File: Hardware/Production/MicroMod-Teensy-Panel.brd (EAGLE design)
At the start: 199.6 x 83.1 mm, 1190 parts, among them J1 MICROMOD-2222, J10 MICROMOD-2222, J11 MICROMOD-2222, J12 MICROMOD-2222, J13 MICROMOD-2222, J14 MICROMOD-2222, J15 MICROMOD-2222, J16 MICROMOD-2222, J2 MICROMOD-2222, J3 MICROMOD-2222, J4 MICROMOD-2222, J5 MICROMOD-2222, J6 MICROMOD-2222, J7 MICROMOD-2222, J8 MICROMOD-2222, J9 MICROMOD-2222, Q1 20V/4.2A/52mΩ/1.4W, Q10 20V/0.2A/8MHz/1.2Ω/1Vth, Q11 20V/4.2A/52mΩ/1.4W, Q12 20V/0.2A/8MHz/1.2Ω/1Vth, Q13 20V/4.2A/52mΩ/1.4W, Q14 20V/0.2A/8MHz/1.2Ω/1Vth, Q15 20V/4.2A/52mΩ/1.4W, Q16 20V/0.2A/8MHz/1.2Ω/1Vth, Q17 20V/4.2A/52mΩ/1.4W, Q18 20V/0.2A/8MHz/1.2Ω/1Vth, Q19 20V/4.2A/52mΩ/1.4W, Q2 20V/0.2A/8MHz/1.2Ω/1Vth, Q20 20V/0.2A/8MHz/1.2Ω/1Vth, Q21 20V/4.2A/52mΩ/1.4W, Q22 20V/0.2A/8MHz/1.2Ω/1Vth, Q23 20V/4.2A/52mΩ/1.4W, Q24 20V/0.2A/8MHz/1.2Ω/1Vth, Q25 20V/4.2A/52mΩ/1.4W, Q26 20V/0.2A/8MHz/1.2Ω/1Vth, Q27 20V/4.2A/52mΩ/1.4W, Q28 20V/0.2A/8MHz/1.2Ω/1Vth, Q29 20V/4.2A/52mΩ/1.4W, Q3 20V/4.2A/52mΩ/1.4W, Q30 20V/0.2A/8MHz/1.2Ω/1Vth, Q31 20V/4.2A/52mΩ/1.4W, Q32 20V/0.2A/8MHz/1.2Ω/1Vth, Q4 20V/0.2A/8MHz/1.2Ω/1Vth, Q5 20V/4.2A/52mΩ/1.4W, Q6 20V/0.2A/8MHz/1.2Ω/1Vth, Q7 20V/4.2A/52mΩ/1.4W, Q8 20V/0.2A/8MHz/1.2Ω/1Vth, Q9 20V/4.2A/52mΩ/1.4W, U1 IMXRT1062DV10X10, U10 IMXRT1062DV10X10, U11 W25QXX3X2, U12 MKL02Z32VFG4, U13 IMXRT1062DV10X10, U14 W25QXX3X2, U15 MKL02Z32VFG4, U16 IMXRT1062DV10X10, U17 W25QXX3X2, U18 MKL02Z32VFG4, U19 IMXRT1062DV10X10, U2 W25QXX3X2, U20 W25QXX3X2, U21 MKL02Z32VFG4, U22 IMXRT1062DV10X10, U23 W25QXX3X2, U24 MKL02Z32VFG4, U25 IMXRT1062DV10X10, U26 W25QXX3X2, U27 MKL02Z32VFG4, U28 IMXRT1062DV10X10, U29 W25QXX3X2, U3 MKL02Z32VFG4, U30 MKL02Z32VFG4, U31 IMXRT1062DV10X10, U32 W25QXX3X2, U33 MKL02Z32VFG4, U34 IMXRT1062DV10X10, U35 W25QXX3X2, U36 MKL02Z32VFG4, U37 IMXRT1062DV10X10, U38 W25QXX3X2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

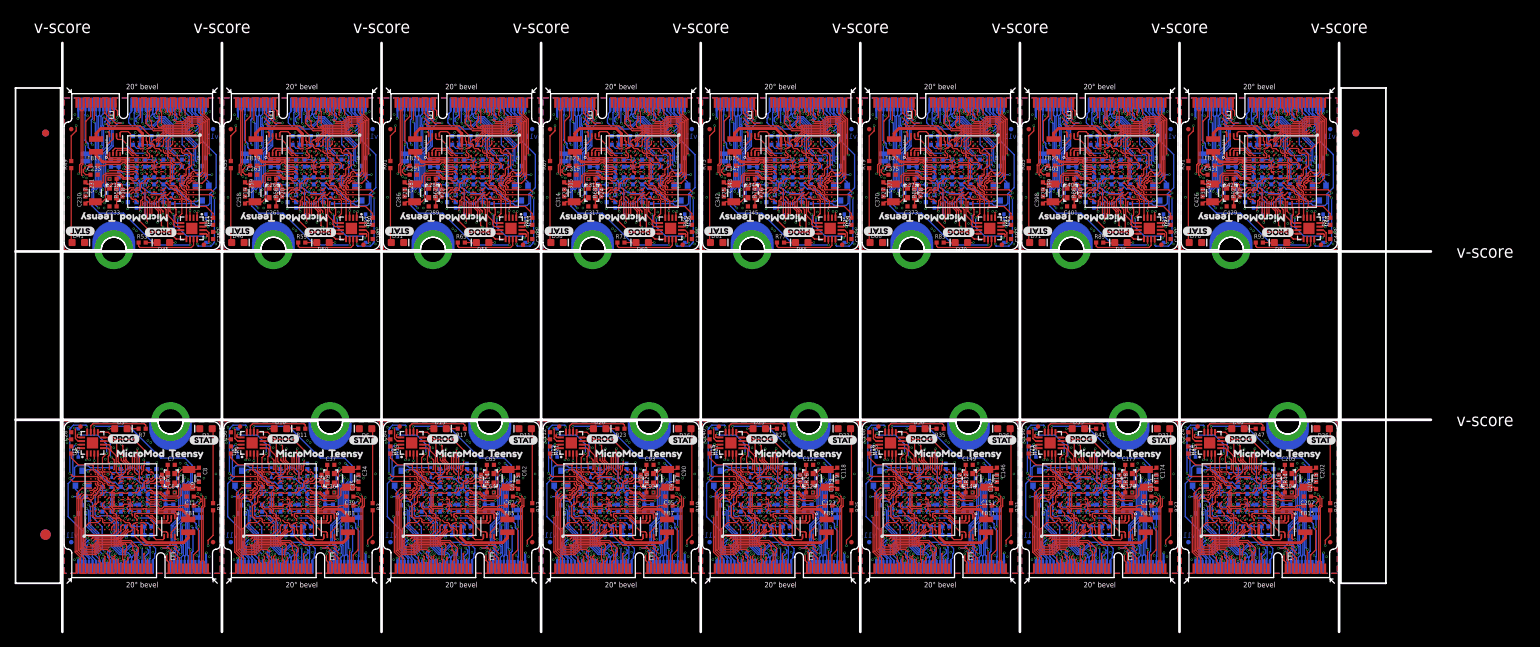
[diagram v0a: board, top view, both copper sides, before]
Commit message: Matches trace lenths to flash. New panel.
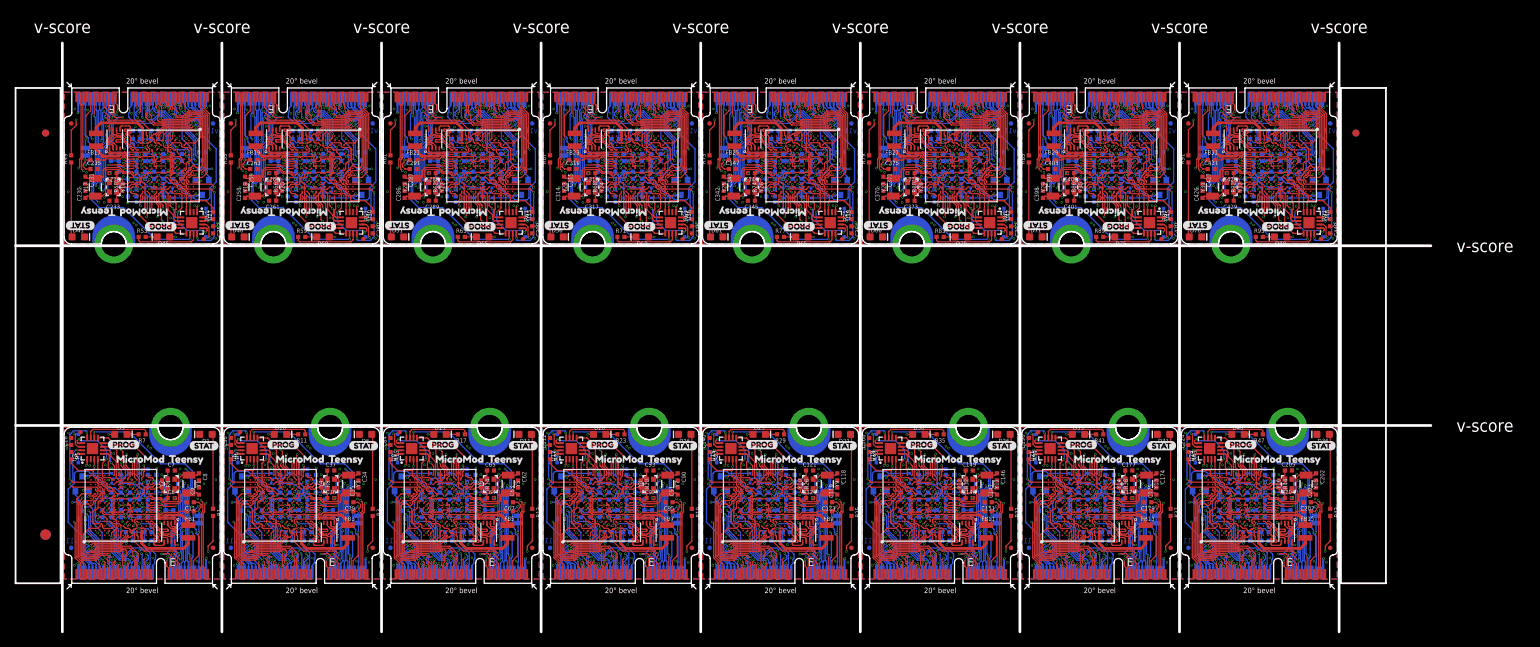
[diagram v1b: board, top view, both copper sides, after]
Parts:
- TP1, TP100, TP111, TP12, TP122, TP133, TP144, TP155, TP166, TP23, TP34, TP45, TP56, TP67, TP78, TP89: value 32kHz Test -> (none)
- TP10, TP101, TP102, TP103, TP104, TP105, TP106, TP107, TP108, TP109, TP11, TP110, TP112, TP113, TP114, TP115, TP116, TP117, TP118, TP119, TP120, TP121, TP123, TP124, TP125, TP126, TP127, TP128, TP129, TP13, TP130, TP131, TP132, TP134, TP135, TP136, TP137, TP138, TP139, TP14, TP140, TP141, TP142, TP143, TP145, TP146, TP147, TP148, TP149, TP15, TP150, TP151, TP152, TP153, TP154, TP156, TP157, TP158, TP159, TP16, TP160, TP161, TP162, TP163, TP164, TP165, TP167, TP168, TP169, TP17, TP170, TP171, TP172, TP173, TP174, TP175, TP176, TP18, TP19, TP2, TP20, TP21, TP22, TP24, TP25, TP26, TP27, TP28, TP29, TP3, TP30, TP31, TP32, TP33, TP35, TP36, TP37, TP38, TP39, TP4, TP40, TP41, TP42, TP43, TP44, TP46, TP47, TP48, TP49, TP5, TP50, TP51, TP52, TP53, TP54, TP55, TP57, TP58, TP59, TP6, TP60, TP61, TP62, TP63, TP64, TP65, TP66, TP68, TP69, TP7, TP70, TP71, TP72, TP73, TP74, TP75, TP76, TP77, TP79, TP8, TP80, TP81, TP82, TP83, TP84, TP85, TP86, TP87, TP88, TP9, TP90, TP91, TP92, TP93, TP94, TP95, TP96, TP97, TP98, TP99: value TEST-POINT2 -> (none)
- moved C11 0.80 mm to (17.8, 11.4)
- moved C112 0.80 mm to (68.5, 20.0)
- moved C118 0.80 mm to (109.0, 15.0)
- moved C119 0.80 mm to (109.0, 13.0)
- moved C120 0.80 mm to (105.1, 12.0)
- moved C123 0.80 mm to (107.8, 11.4)
- moved C140 0.80 mm to (91.0, 20.0)
- moved C146 0.80 mm to (131.5, 15.0)
- moved C147 0.80 mm to (131.5, 13.0)
- moved C148 0.80 mm to (127.6, 12.0)
- moved C151 0.80 mm to (130.3, 11.4)
- moved C168 0.80 mm to (113.5, 20.0)
- moved C174 0.80 mm to (154.1, 15.0)
- moved C175 0.80 mm to (154.1, 13.0)
- moved C176 0.80 mm to (150.2, 12.0)
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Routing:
- net QSPI6: track 3.16 -> 7.39 mm
- net QSPI42: track 3.16 -> 7.39 mm
- net QSPI62: track 3.16 -> 7.39 mm
- net QSPI58: track 3.16 -> 7.39 mm
- net QSPI34: track 3.16 -> 7.39 mm
- net QSPI30: track 3.16 -> 7.39 mm
- net QSPI26: track 3.16 -> 7.39 mm
- net QSPI2: track 3.16 -> 7.39 mm
- net QSPI38: track 3.16 -> 7.39 mm
- net QSPI10: track 3.16 -> 7.39 mm
- net QSPI50: track 3.16 -> 7.39 mm
- net QSPI18: track 3.16 -> 7.39 mm
- net QSPI54: track 3.16 -> 7.39 mm
- net QSPI46: track 3.16 -> 7.39 mm
- net QSPI22: track 3.16 -> 7.39 mm
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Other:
- outline, holes or cut-outs redrawn

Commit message: Route bus pins to v11.
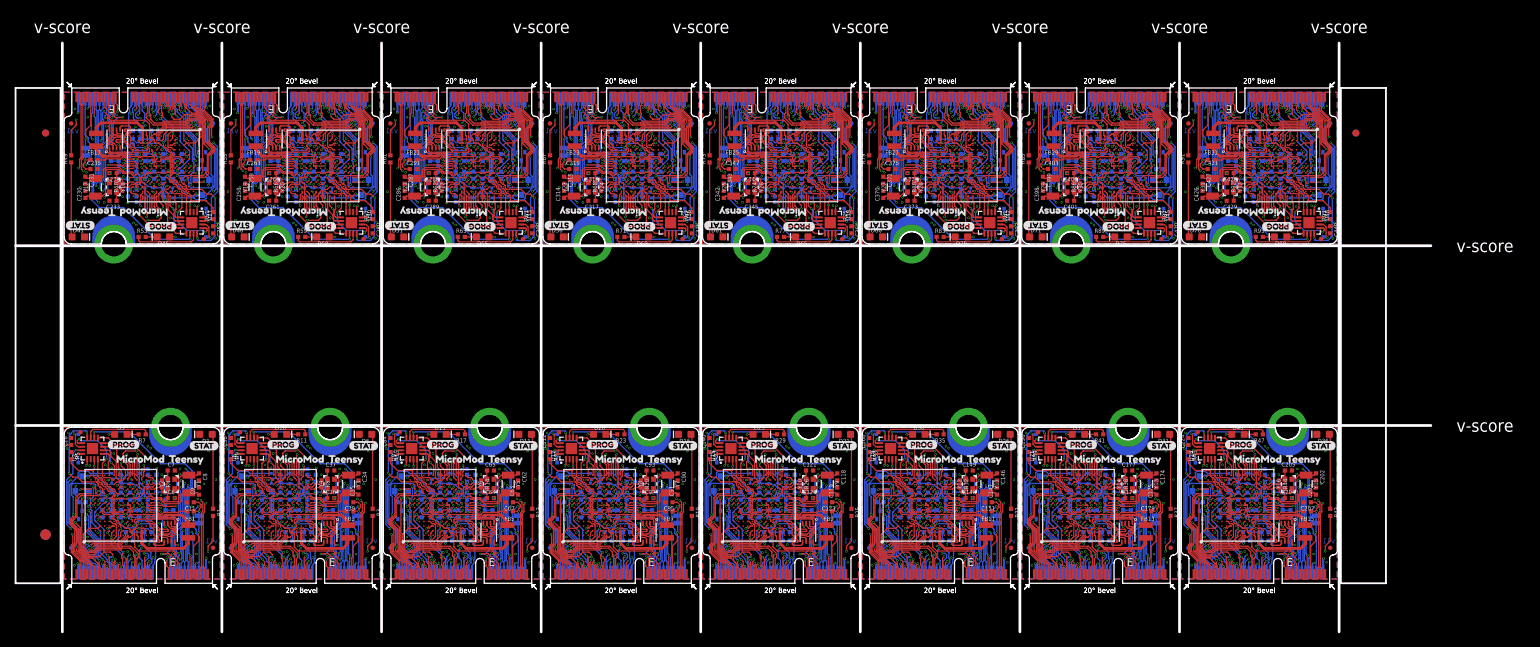
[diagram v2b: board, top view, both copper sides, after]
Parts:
- added FRAME1, FRAME10, FRAME11, FRAME12, FRAME13, FRAME14, FRAME15, FRAME16, FRAME2, FRAME3, FRAME4, FRAME5, FRAME6, FRAME7, FRAME8, FRAME9: FRAME-LEDGER, SparkFun-Aesthetics:CREATIVE_COMMONS
- added LOGO17, LOGO19, LOGO21, LOGO23, LOGO25, LOGO27, LOGO29, LOGO31: SFE_LOGO_NAME_FLAME.1_INCH, SparkFun-Aesthetics:SFE_LOGO_NAME_FLAME_.1
- added LOGO18, LOGO20, LOGO22, LOGO24, LOGO26, LOGO28, LOGO30, LOGO32: OSHW-LOGONO_SILK, SparkFun-Aesthetics:DUMMY
- LOGO10, LOGO12, LOGO14, LOGO16, LOGO2, LOGO4, LOGO6, LOGO8: value SFE_LOGO_NAME_FLAME.1_INCH -> OSHW-LOGONO_SILK; device SparkFun-Aesthetics:SFE_LOGO_NAME_FLAME_.1 -> SparkFun-Aesthetics:DUMMY
- moved LOGO8 116.0 mm to (55.7, -22.9), flipped to the top
- moved LOGO6 95.3 mm to (33.2, -22.9), flipped to the top
- moved LOGO9 88.1 mm to (96.7, 18.1), turned to 0 degrees
- moved LOGO10 84.8 mm to (78.2, -22.9), flipped to the top, turned to 0 degrees
- moved LOGO16 79.4 mm to (145.7, -22.9), flipped to the top, turned to 0 degrees
- moved LOGO12 76.7 mm to (100.7, -22.9), flipped to the top, turned to 0 degrees
- moved LOGO4 75.6 mm to (10.7, -22.9), flipped to the top
- moved LOGO14 74.8 mm to (123.2, -22.9), flipped to the top, turned to 0 degrees
- moved LOGO11 67.9 mm to (119.2, 18.1), turned to 0 degrees
- moved LOGO7 67.5 mm to (74.2, 18.1)
- moved LOGO2 58.0 mm to (-11.8, -22.9), flipped to the top
- moved LOGO13 49.6 mm to (141.8, 18.1), turned to 0 degrees
- moved LOGO5 45.0 mm to (51.7, 18.1)
- moved LOGO15 36.4 mm to (164.3, 18.1), turned to 0 degrees
- moved LOGO3 22.5 mm to (29.2, 18.1)
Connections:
- new net GPIO/100: J10.69, U28.A10
- new net GPIO/101: J10.71, U28.D9
- new net GPIO/102: U28.D5
- new net GPIO/103: J10.65, U28.C10
- new net GPIO/104: J10.63, U28.H4
- new net GPIO/105: J10.40, U28.C8
- new net GPIO/106: J10.42, U28.B8
- new net GPIO/107: J10.44, U28.A8
- new net GPIO/108: J10.46, U28.A9
- new net GPIO/109: J10.48, U28.B9
- new net GPIO/110: J10.73, U28.C9
- new net GPIO/111: J11.69, U31.A10
- new net GPIO/112: J11.71, U31.D9
- new net GPIO/113: U31.D5
- new net GPIO/114: J11.65, U31.C10
- new net GPIO/115: J11.63, U31.H4
- new net GPIO/116: J11.40, U31.C8
- new net GPIO/117: J11.42, U31.B8
- new net GPIO/118: J11.44, U31.A8
- new net GPIO/119: J11.46, U31.A9
- new net GPIO/120: J11.48, U31.B9
- new net GPIO/121: J11.73, U31.C9
- new net GPIO/122: J12.69, U34.A10
- new net GPIO/123: J12.71, U34.D9
- new net GPIO/124: U34.D5
- new net GPIO/125: J12.65, U34.C10
- new net GPIO/126: J12.63, U34.H4
- new net GPIO/127: J12.40, U34.C8
- new net GPIO/128: J12.42, U34.B8
- new net GPIO/129: J12.44, U34.A8
- new net GPIO/130: J12.46, U34.A9
- new net GPIO/131: J12.48, U34.B9
- new net GPIO/132: J12.73, U34.C9
- new net GPIO/133: J13.69, U37.A10
- new net GPIO/134: J13.71, U37.D9
- new net GPIO/135: U37.D5
- new net GPIO/136: J13.65, U37.C10
- new net GPIO/137: J13.63, U37.H4
- new net GPIO/138: J13.40, U37.C8
- new net GPIO/139: J13.42, U37.B8
- new net GPIO/140: J13.44, U37.A8
- new net GPIO/141: J13.46, U37.A9
- new net GPIO/142: J13.48, U37.B9
- new net GPIO/143: J13.73, U37.C9
- new net GPIO/144: J14.69, U40.A10
- new net GPIO/145: J14.71, U40.D9
- new net GPIO/146: U40.D5
- new net GPIO/147: J14.65, U40.C10
- new net GPIO/148: J14.63, U40.H4
- new net GPIO/149: J14.40, U40.C8
- new net GPIO/150: J14.42, U40.B8
- new net GPIO/151: J14.44, U40.A8
- new net GPIO/152: J14.46, U40.A9
- new net GPIO/153: J14.48, U40.B9
- new net GPIO/154: J14.73, U40.C9
- new net GPIO/155: J15.69, U43.A10
- new net GPIO/156: J15.71, U43.D9
- new net GPIO/157: U43.D5
- new net GPIO/158: J15.65, U43.C10
- new net GPIO/159: J15.63, U43.H4
- new net GPIO/160: J15.40, U43.C8
- new net GPIO/161: J15.42, U43.B8
- new net GPIO/162: J15.44, U43.A8
- new net GPIO/163: J15.46, U43.A9
- new net GPIO/164: J15.48, U43.B9
- new net GPIO/165: J15.73, U43.C9
- new net GPIO/166: J16.69, U46.A10
- new net GPIO/167: J16.71, U46.D9
- new net GPIO/168: U46.D5
- new net GPIO/169: J16.65, U46.C10
- new net GPIO/170: J16.63, U46.H4
- new net GPIO/171: J16.40, U46.C8
- new net GPIO/172: J16.42, U46.B8
- new net GPIO/173: J16.44, U46.A8
- new net GPIO/174: J16.46, U46.A9
- new net GPIO/175: J16.48, U46.B9
- new net GPIO/176: J16.73, U46.C9
- new net GPIO/81: J8.65, U22.C10
- new net GPIO/82: J8.63, U22.H4
- new net GPIO/83: J8.40, U22.C8
- new net GPIO/84: J8.42, U22.B8
- new net GPIO/85: J8.44, U22.A8
- new net GPIO/86: J8.46, U22.A9
- new net GPIO/87: J8.48, U22.B9
- new net GPIO/88: J8.73, U22.C9
- new net GPIO/89: J9.69, U25.A10
- new net GPIO/90: J9.71, U25.D9
- new net GPIO/91: U25.D5
- new net GPIO/92: J9.65, U25.C10
- new net GPIO/93: J9.63, U25.H4
- new net GPIO/94: J9.40, U25.C8
- new net GPIO/95: J9.42, U25.B8
- new net GPIO/96: J9.44, U25.A8
- new net GPIO/97: J9.46, U25.A9
- new net GPIO/98: J9.48, U25.B9
- new net GPIO/99: J9.73, U25.C9
- net GPIO/1: now also J2.69; no longer J2.71
- net GPIO/10: now also J2.44, U4.A8; no longer J3.46, U7.D5
- net GPIO/11: now also J2.46, U4.A9; no longer J3.48, U7.C10
- net GPIO/12: now also J2.48, U4.B9; no longer J3.73, U7.H4
- net GPIO/13: now also J2.73, U4.C9; no longer J4.71, U10.A10
- net GPIO/14: now also J3.69, U7.A10; no longer J4.40, U10.D9
- net GPIO/15: now also J3.71, U7.D9; no longer J4.46, U10.D5
- net GPIO/16: now also U7.D5; no longer J4.48, U10.C10
- net GPIO/17: now also J3.65, U7.C10; no longer J4.73, U10.H4
- net GPIO/18: now also J3.63, U7.H4; no longer J5.71, U13.A10
- net GPIO/19: now also J3.40, U7.C8; no longer J5.40, U13.D9
- net GPIO/2: now also J2.71; no longer J2.40
- net GPIO/20: now also J3.42, U7.B8; no longer J5.46, U13.D5
- net GPIO/21: now also J3.44, U7.A8; no longer J5.48, U13.C10
- net GPIO/22: now also J3.46, U7.A9; no longer J5.73, U13.H4
- net GPIO/23: now also J3.48, U7.B9; no longer J6.71, U16.A10
- net GPIO/24: now also J3.73, U7.C9; no longer J6.40, U16.D9
- net GPIO/25: now also J4.69, U10.A10; no longer J6.46, U16.D5
- net GPIO/26: now also J4.71, U10.D9; no longer J6.48, U16.C10
- net GPIO/26/A1: now also J2.67; no longer J2.42
- net GPIO/26/A10: now also J11.67; no longer J11.42
- net GPIO/26/A11: now also J12.67; no longer J12.42
- net GPIO/26/A12: now also J1.67; no longer J1.42
- net GPIO/26/A13: now also J13.67; no longer J13.42
- net GPIO/26/A14: now also J14.67; no longer J14.42
- net GPIO/26/A15: now also J15.67; no longer J15.42
- net GPIO/26/A16: now also J16.67; no longer J16.42
- net GPIO/26/A2: now also J3.67; no longer J3.42
- net GPIO/26/A3: now also J4.67; no longer J4.42
- net GPIO/26/A4: now also J5.67; no longer J5.42
- net GPIO/26/A5: now also J6.67; no longer J6.42
- net GPIO/26/A6: now also J7.67; no longer J7.42
- net GPIO/26/A7: now also J8.67; no longer J8.42
- net GPIO/26/A8: now also J9.67; no longer J9.42
- net GPIO/26/A9: now also J10.67; no longer J10.42
- net GPIO/27: now also U10.D5; no longer J6.73, U16.H4
- net GPIO/27/A1: now also J2.8; no longer J2.44
- net GPIO/27/A10: now also J11.8; no longer J11.44
- net GPIO/27/A11: now also J12.8; no longer J12.44
- net GPIO/27/A12: now also J13.8; no longer J13.44
- net GPIO/27/A13: now also J1.8; no longer J1.44
- net GPIO/27/A14: now also J14.8; no longer J14.44
- net GPIO/27/A15: now also J15.8; no longer J15.44
- net GPIO/27/A16: now also J16.8; no longer J16.44
- net GPIO/27/A2: now also J3.8; no longer J3.44
- net GPIO/27/A3: now also J4.8; no longer J4.44
- net GPIO/27/A4: now also J5.8; no longer J5.44
- net GPIO/27/A5: now also J6.8; no longer J6.44
- net GPIO/27/A6: now also J7.8; no longer J7.44
- net GPIO/27/A7: now also J8.8; no longer J8.44
- net GPIO/27/A8: now also J9.8; no longer J9.44
- net GPIO/27/A9: now also J10.8; no longer J10.44
- net GPIO/28: no longer J1.46
- net GPIO/29: now also J4.65, U10.C10; no longer J7.71, U19.A10
- net GPIO/3: no longer J2.46
- net GPIO/30: now also J4.63, U10.H4; no longer J7.40, U19.D9
- net GPIO/31: now also J4.40, U10.C8; no longer J7.46, U19.D5
- net GPIO/32: now also J1.65; no longer J1.48
- net GPIO/33: now also J1.63; no longer J1.73
- net GPIO/34: now also J4.42, U10.B8; no longer J7.48, U19.C10
- net GPIO/35: now also J4.44, U10.A8; no longer J7.73, U19.H4
- net GPIO/36: now also J4.46, U10.A9; no longer J8.71, U22.A10
- net GPIO/37: now also J4.48, U10.B9; no longer J8.40, U22.D9
- net GPIO/38: now also J4.73, U10.C9; no longer J8.46, U22.D5
- net GPIO/39: now also J5.69, U13.A10; no longer J8.48, U22.C10
- net GPIO/4: now also J2.65; no longer J2.48
- net GPIO/40: now also J1.40, U1.C8; no longer J8.73, U22.H4
- net GPIO/41: now also J1.42, U1.B8; no longer J9.71, U25.A10
- net GPIO/42: now also J1.44, U1.A8; no longer J9.40, U25.D9
- net GPIO/43: now also J1.46, U1.A9; no longer J9.46, U25.D5
- net GPIO/44: now also J1.48, U1.B9; no longer J9.48, U25.C10
- net GPIO/45: now also J1.73, U1.C9; no longer J9.73, U25.H4
- net GPIO/46: now also J5.71, U13.D9; no longer J10.71, U28.A10
- net GPIO/47: now also U13.D5; no longer J10.40, U28.D9
- net GPIO/48: now also J5.65, U13.C10; no longer J10.46, U28.D5
- net GPIO/49: now also J5.63, U13.H4; no longer J10.48, U28.C10
- net GPIO/5: now also J2.63; no longer J2.73
- net GPIO/50: now also J5.40, U13.C8; no longer J10.73, U28.H4
- net GPIO/51: now also J5.42, U13.B8; no longer J11.71, U31.A10
- net GPIO/52: now also J5.44, U13.A8; no longer J11.40, U31.D9
- net GPIO/53: now also J5.46, U13.A9; no longer J11.46, U31.D5
- net GPIO/54: now also J5.48, U13.B9; no longer J11.48, U31.C10
- net GPIO/55: now also J5.73, U13.C9; no longer J11.73, U31.H4
- net GPIO/56: now also J6.69, U16.A10; no longer J12.71, U34.A10
- net GPIO/57: now also J6.71, U16.D9; no longer J12.40, U34.D9
- net GPIO/58: now also U16.D5; no longer J12.46, U34.D5
- net GPIO/59: now also J6.65, U16.C10; no longer J12.48, U34.C10
- net GPIO/6: now also J1.71; no longer J1.40
- net GPIO/60: now also J6.63, U16.H4; no longer J12.73, U34.H4
- net GPIO/61: now also J6.40, U16.C8; no longer J13.71, U37.A10
- net GPIO/62: now also J6.42, U16.B8; no longer J13.40, U37.D9
- net GPIO/63: now also J6.44, U16.A8; no longer J13.46, U37.D5
- net GPIO/64: now also J6.46, U16.A9; no longer J13.48, U37.C10
- net GPIO/65: now also J6.48, U16.B9; no longer J13.73, U37.H4
- net GPIO/66: now also J6.73, U16.C9; no longer J14.71, U40.A10
- net GPIO/67: now also J7.69, U19.A10; no longer J14.40, U40.D9
- net GPIO/68: now also J7.71, U19.D9; no longer J14.46, U40.D5
- net GPIO/69: now also U19.D5; no longer J14.48, U40.C10
- net GPIO/7: now also J2.40, U4.C8; no longer J3.71, U7.A10
- net GPIO/70: now also J7.65, U19.C10; no longer J14.73, U40.H4
- net GPIO/71: now also J7.63, U19.H4; no longer J15.71, U43.A10
- net GPIO/72: now also J7.40, U19.C8; no longer J15.40, U43.D9
- net GPIO/73: now also J7.42, U19.B8; no longer J15.46, U43.D5
- net GPIO/74: now also J7.44, U19.A8; no longer J15.48, U43.C10
- net GPIO/75: now also J7.46, U19.A9; no longer J15.73, U43.H4
- net GPIO/76: now also J7.48, U19.B9; no longer J16.71, U46.A10
- net GPIO/77: now also J7.73, U19.C9; no longer J16.40, U46.D9
- net GPIO/78: now also J8.69, U22.A10; no longer J16.46, U46.D5
- net GPIO/79: now also J8.71, U22.D9; no longer J16.48, U46.C10
- net GPIO/8: now also J2.42, U4.B8; no longer J3.40, U7.D9
- net GPIO/80: now also U22.D5; no longer J16.73, U46.H4
- net GPIO/9: now also J1.69; no longer J1.71
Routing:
- net GPIO/98: track 0.00 -> 29.3 mm, vias 0 -> 2
- net GPIO/164: track 0.00 -> 29.3 mm, vias 0 -> 2
- net GPIO/153: track 0.00 -> 29.3 mm, vias 0 -> 2
- net GPIO/142: track 0.00 -> 29.3 mm, vias 0 -> 2
- net GPIO/131: track 0.00 -> 29.3 mm, vias 0 -> 2
- net GPIO/109: track 0.00 -> 29.3 mm, vias 0 -> 2
- net GPIO/175: track 0.00 -> 29.3 mm, vias 0 -> 2
- net GPIO/120: track 0.00 -> 29.3 mm, vias 0 -> 2
- net GPIO/87: track 0.00 -> 29.3 mm, vias 0 -> 2
- net GPIO/130: track 0.00 -> 26.1 mm, vias 0 -> 2
- net GPIO/97: track 0.00 -> 26.1 mm, vias 0 -> 2
- net GPIO/152: track 0.00 -> 26.1 mm, vias 0 -> 2
- net GPIO/119: track 0.00 -> 26.1 mm, vias 0 -> 2
- net GPIO/108: track 0.00 -> 26.1 mm, vias 0 -> 2
- net GPIO/86: track 0.00 -> 26.1 mm, vias 0 -> 2
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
